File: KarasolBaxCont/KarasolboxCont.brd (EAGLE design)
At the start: 44.1 x 76.2 mm, 28 parts, among them IC1 REG1117, IC2 7808DT, J1 POWER_JACKTOE, Q4 IRF3707S

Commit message: fix
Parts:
- moved CR1 1.27 mm to (30.5, 21.6), turned to 270 degrees
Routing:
- net GND: track 210.1 -> 220.7 mm, vias 1 -> 0
- net D10: track 17.9 -> 13.6 mm
- net VCCSRV: track 82.7 -> 86.8 mm
- net D11: track 19.8 -> 23.5 mm
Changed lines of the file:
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@@
 <element name="PC2" library="SparkFun-Capacitors" package="0805" value="0.1uf" x="26.67" y="59.69" rot="R270"/>
 <element name="CD1" library="SparkFun-DiscreteSemi" package="SMA-DIODE" value="" x="20.32" y="11.43" rot="R180"/>
-<element name="CR1" library="SparkFun-Passives" package="0805" value="1K" x="30.48" y="20.32" rot="R180"/>
+<element name="CR1" library="SparkFun-Passives" package="0805" value="1K" x="30.48" y="21.59" rot="R270"/>
 <element name="PD1" library="SparkFun-DiscreteSemi" package="SMA-DIODE" value="" x="26.67" y="71.12" rot="R90"/>
 <element name="MD2" library="SparkFun-DiscreteSemi" package="SMA-DIODE" value="" x="29.21" y="29.21"/>
@@
 <wire x1="38.8" y1="69.6" x2="39" y2="69.85" width="0.8" layer="1"/>
 <wire x1="38.4" y1="61.2" x2="38.06" y2="60.96" width="0.8" layer="1"/>
-<wire x1="33.6" y1="26.4" x2="35.2" y2="28" width="0.8" layer="1"/>
-<wire x1="33.2" y1="26.4" x2="33.6" y2="26.4" width="0.8" layer="1"/>
-<wire x1="33.2" y1="25.6" x2="33.2" y2="26.4" width="0.8" layer="16"/>
-<wire x1="39.6" y1="19.2" x2="33.4" y2="25.4" width="0.8" layer="16"/>
-<wire x1="33.4" y1="25.4" x2="33.2" y2="25.6" width="0.8" layer="16"/>
-<wire x1="40.4" y1="19.2" x2="39.6" y2="19.2" width="0.8" layer="16"/>
+<wire x1="30.8" y1="23.6" x2="30.8" y2="22.8" width="0.8" layer="1"/>
+<wire x1="35.2" y1="28" x2="30.8" y2="23.6" width="0.8" layer="1"/>
+<wire x1="30.8" y1="22.8" x2="30.48" y2="22.49" width="0.8" layer="1"/>
 <wire x1="35.2" y1="28" x2="35.56" y2="28.31" width="0.8" layer="1"/>
-<wire x1="40.4" y1="19.2" x2="40.64" y2="19.09" width="0.8" layer="16"/>
 <wire x1="31.2" y1="13.2" x2="28" y2="16.4" width="0.8" layer="1"/>
 <wire x1="34.8" y1="13.2" x2="31.2" y2="13.2" width="0.8" layer="1"/>
-<wire x1="40.4" y1="18.8" x2="34.8" y2="13.2" width="0.8" layer="1"/>
+<wire x1="40.4" y1="18.8" x2="38.2" y2="16.6" width="0.8" layer="1"/>
+<wire x1="38.2" y1="16.6" x2="34.8" y2="13.2" width="0.8" layer="1"/>
 <wire x1="28" y1="16.4" x2="27.94" y2="16.51" width="0.8" layer="1"/>
 <wire x1="40.4" y1="18.8" x2="40.64" y2="19.09" width="0.8" layer="1"/>
+<wire x1="32" y1="22.8" x2="30.8" y2="22.8" width="0.8" layer="1"/>
+<wire x1="38.2" y1="16.6" x2="32" y2="22.8" width="0.8" layer="1"/>
 <wire x1="16.8" y1="56.4" x2="16.8" y2="55.2" width="0.8" layer="1"/>
 <wire x1="16.8" y1="55.2" x2="16.8" y2="52.4" width="0.8" layer="1"/>
@@
 <wire x1="8" y1="39.2" x2="7.62" y2="39.37" width="0.8" layer="16"/>
 <wire x1="16" y1="26.8" x2="16.14" y2="26.67" width="0.8" layer="16"/>
-<wire x1="15.6" y1="51.2" x2="31.6" y2="51.2" width="0.8" layer="16"/>
-<wire x1="10" y1="45.6" x2="15.6" y2="51.2" width="0.8" layer="16"/>
-<wire x1="10" y1="40.4" x2="10" y2="45.6" width="0.8" layer="16"/>
+<wire x1="30.4" y1="51.6" x2="31.6" y2="51.6" width="0.8" layer="16"/>
+<wire x1="25.6" y1="56.4" x2="30.4" y2="51.6" width="0.8" layer="16"/>
+<wire x1="24" y1="56.4" x2="25.6" y2="56.4" width="0.8" layer="16"/>
+<wire x1="10" y1="42.4" x2="24" y2="56.4" width="0.8" layer="16"/>
+<wire x1="10" y1="40.4" x2="10" y2="42.4" width="0.8" layer="16"/>
 <wire x1="8.6" y1="39" x2="10" y2="40.4" width="0.8" layer="16"/>
-<wire x1="31.6" y1="51.2" x2="31.735" y2="51.5125" width="0.8" layer="16"/>
+<wire x1="31.6" y1="51.6" x2="31.735" y2="51.5125" width="0.8" layer="16"/>
 <wire x1="10" y1="40.8" x2="10" y2="55.2" width="0.8" layer="1"/>
 <wire x1="8.8" y1="39.6" x2="10" y2="40.8" width="0.8" layer="1"/>
 <wire x1="8" y1="39.6" x2="8.8" y2="39.6" width="0.8" layer="1"/>
 <wire x1="8" y1="39.6" x2="7.62" y2="39.37" width="0.8" layer="1"/>
-<wire x1="32.4" y1="25.2" x2="33.2" y2="25.2" width="0.8" layer="16"/>
-<wire x1="24" y1="16.8" x2="32.4" y2="25.2" width="0.8" layer="16"/>
+<wire x1="26" y1="18.8" x2="40.4" y2="18.8" width="0.8" layer="16"/>
+<wire x1="24" y1="16.8" x2="26" y2="18.8" width="0.8" layer="16"/>
 <wire x1="21.6" y1="16.8" x2="24" y2="16.8" width="0.8" layer="16"/>
 <wire x1="18" y1="20.4" x2="21.6" y2="16.8" width="0.8" layer="16"/>
 <wire x1="18" y1="21.2" x2="18" y2="20.4" width="0.8" layer="16"/>
-<wire x1="33.2" y1="25.2" x2="33.4" y2="25.4" width="0.8" layer="16"/>
+<wire x1="40.4" y1="18.8" x2="40.64" y2="19.09" width="0.8" layer="16"/>
 <wire x1="18" y1="21.2" x2="17.78" y2="21.59" width="0.8" layer="16"/>
 <wire x1="8" y1="60.4" x2="26.4" y2="60.4" width="0.8" layer="1"/>
 <wire x1="26.4" y1="60.4" x2="26.67" y2="60.59" width="0.8" layer="1"/>
-<via x="33.2" y="26.4" extent="1-16" drill="0.8"/>
-<wire x1="32.4" y1="25.2" x2="31.38" y2="20.32" width="0" layer="19" extent="1-16"/>
 </signal>
 <signal name="RAW" class="1">
@@
 <wire x1="13.6" y1="57.2" x2="13.6" y2="57.15" width="0.8" layer="1"/>
 <wire x1="18.8" y1="56.8" x2="19.0754" y2="56.5404" width="0.8" layer="1"/>
-<wire x1="18.8" y1="56.4" x2="18.8" y2="52.4" width="0.8" layer="1"/>
+<wire x1="18.8" y1="56.4" x2="18.8" y2="54" width="0.8" layer="1"/>
+<wire x1="18.8" y1="54" x2="18.8" y2="52.4" width="0.8" layer="1"/>
 <wire x1="18.8" y1="52.4" x2="18.68" y2="52.07" width="0.8" layer="1"/>
 <wire x1="18.8" y1="56.4" x2="19.0754" y2="56.5404" width="0.8" layer="1"/>
@@
 <wire x1="33.8" y1="47.8" x2="35.2" y2="46.4" width="0.8" layer="1"/>
 <wire x1="39.2" y1="48.8" x2="39.355" y2="48.9725" width="0.8" layer="1"/>
-<wire x1="18.8" y1="51.2" x2="18.8" y2="52" width="0.8" layer="1"/>
-<wire x1="16.4" y1="48.8" x2="18.8" y2="51.2" width="0.8" layer="1"/>
-<wire x1="16.4" y1="45.2" x2="16.4" y2="48.8" width="0.8" layer="16"/>
-<wire x1="22" y1="39.6" x2="16.4" y2="45.2" width="0.8" layer="16"/>
-<wire x1="22.8" y1="39.6" x2="22" y2="39.6" width="0.8" layer="16"/>
-<wire x1="18.8" y1="52" x2="18.68" y2="52.07" width="0.8" layer="1"/>
-<wire x1="22.8" y1="39.6" x2="22.86" y2="39.37" width="0.8" layer="16"/>
+<wire x1="24.8" y1="54" x2="18.8" y2="54" width="0.8" layer="1"/>
+<wire x1="24.8" y1="52.4" x2="24.8" y2="54" width="0.8" layer="16"/>
+<wire x1="30.8" y1="46.4" x2="24.8" y2="52.4" width="0.8" layer="16"/>
+<wire x1="32.4" y1="46.4" x2="30.8" y2="46.4" width="0.8" layer="16"/>
+<wire x1="34" y1="48" x2="32.4" y2="46.4" width="0.8" layer="16"/>
+<wire x1="34" y1="48.8" x2="34" y2="48" width="0.8" layer="16"/>
+<wire x1="34" y1="48.8" x2="34.275" y2="48.9725" width="0.8" layer="16"/>
 <wire x1="38.8" y1="24.4" x2="40.4" y2="24.4" width="0.8" layer="16"/>
 <wire x1="24" y1="39.2" x2="38.8" y2="24.4" width="0.8" layer="16"/>
@@
 <wire x1="40.4" y1="24.4" x2="40.64" y2="24.09" width="0.8" layer="16"/>
 <wire x1="23.2" y1="39.2" x2="22.86" y2="39.37" width="0.8" layer="16"/>
-<via x="16.4" y="48.8" extent="1-16" drill="0.8"/>
+<via x="24.8" y="54" extent="1-16" drill="0.8"/>
 </signal>
 <signal name="N$3">
@@
 <contactref element="U$1" pad="D10"/>
 <contactref element="CQ1" pad="1"/>
-<wire x1="24.4" y1="20" x2="29.2" y2="20" width="0.8" layer="1"/>
-<wire x1="23.2" y1="18.8" x2="24.4" y2="20" width="0.8" layer="1"/>
-<wire x1="29.2" y1="20" x2="29.58" y2="20.32" width="0.8" layer="1"/>
-<wire x1="23.2" y1="18.8" x2="22.86" y2="19.05" width="0.8" layer="1"/>
-<wire x1="33.2" y1="21.2" x2="33.2" y2="16.8" width="0.8" layer="1"/>
-<wire x1="32" y1="22.4" x2="33.2" y2="21.2" width="0.8" layer="1"/>
-<wire x1="30.4" y1="22.4" x2="32" y2="22.4" width="0.8" layer="1"/>
-<wire x1="29.6" y1="21.6" x2="30.4" y2="22.4" width="0.8" layer="1"/>
-<wire x1="29.6" y1="20.4" x2="29.6" y2="21.6" width="0.8" layer="1"/>
-<wire x1="33.2" y1="16.8" x2="33.02" y2="16.51" width="0.8" layer="1"/>
-<wire x1="29.6" y1="20.4" x2="29.58" y2="20.32" width="0.8" layer="1"/>
+<wire x1="30.8" y1="18.8" x2="30.8" y2="20.4" width="0.8" layer="1"/>
+<wire x1="32.8" y1="16.8" x2="30.8" y2="18.8" width="0.8" layer="1"/>
+<wire x1="30.8" y1="20.4" x2="30.48" y2="20.69" width="0.8" layer="1"/>
+<wire x1="32.8" y1="16.8" x2="33.02" y2="16.51" width="0.8" layer="1"/>
+<wire x1="25.6" y1="19.2" x2="23.2" y2="19.2" width="0.8" layer="1"/>
+<wire x1="26.8" y1="20.4" x2="25.6" y2="19.2" width="0.8" layer="1"/>
+<wire x1="30.4" y1="20.4" x2="26.8" y2="20.4" width="0.8" layer="1"/>
+<wire x1="23.2" y1="19.2" x2="22.86" y2="19.05" width="0.8" layer="1"/>
+<wire x1="30.4" y1="20.4" x2="30.48" y2="20.69" width="0.8" layer="1"/>
 </signal>
 <signal name="D11">
@@
 <wire x1="35.6" y1="23.2" x2="35.56" y2="23.23" width="0.8" layer="1"/>
 <wire x1="40.4" y1="21.6" x2="40.64" y2="21.59" width="0.8" layer="1"/>
-<wire x1="27.2" y1="21.6" x2="23.2" y2="21.6" width="0.8" layer="1"/>
-<wire x1="29.6" y1="24" x2="27.2" y2="21.6" width="0.8" layer="1"/>
-<wire x1="33.6" y1="24" x2="29.6" y2="24" width="0.8" layer="1"/>
-<wire x1="34.4" y1="23.2" x2="33.6" y2="24" width="0.8" layer="1"/>
-<wire x1="35.2" y1="23.2" x2="34.4" y2="23.2" width="0.8" layer="1"/>
-<wire x1="23.2" y1="21.6" x2="22.86" y2="21.59" width="0.8" layer="1"/>
-<wire x1="35.2" y1="23.2" x2="35.56" y2="23.23" width="0.8" layer="1"/>
+<wire x1="40.4" y1="21.6" x2="23.2" y2="21.6" width="0.8" layer="16"/>
+<wire x1="23.2" y1="21.6" x2="22.86" y2="21.59" width="0.8" layer="16"/>
+<wire x1="40.4" y1="21.6" x2="40.64" y2="21.59" width="0.8" layer="16"/>
 </signal>
 <signal name="D3">
@@
 <wire x1="18.8" y1="47.2" x2="8.4" y2="36.8" width="0.8" layer="1"/>
 <wire x1="18.8" y1="48.8" x2="18.8" y2="47.2" width="0.8" layer="1"/>
-<wire x1="24" y1="54" x2="18.8" y2="48.8" width="0.8" layer="1"/>
-<wire x1="37.6" y1="54" x2="24" y2="54" width="0.8" layer="1"/>
+<wire x1="21.6" y1="51.6" x2="18.8" y2="48.8" width="0.8" layer="1"/>
+<wire x1="28.4" y1="51.6" x2="21.6" y2="51.6" width="0.8" layer="1"/>
+<wire x1="30.8" y1="54" x2="28.4" y2="51.6" width="0.8" layer="1"/>
+<wire x1="37.6" y1="54" x2="30.8" y2="54" width="0.8" layer="1"/>
 <wire x1="39.2" y1="52.4" x2="37.6" y2="54" width="0.8" layer="1"/>
 <wire x1="39.2" y1="51.6" x2="39.2" y2="52.4" width="0.8" layer="1"/>

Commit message: son
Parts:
- added U$2: (no value), Logo:IOTECH_COPPER_M
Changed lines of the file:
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@@
 <element name="CQ1" library="transistor-power" package="D2PACK" value="IRF3707S" x="30.48" y="7.62" rot="R180"/>
 <element name="U$1" library="Arduino-Clk" package="ABK-PRO-MINI" value="ABK-PRO-MINI" x="12.7" y="40.64"/>
+<element name="U$2" library="Logo" package="IOTECH_COPPER_M" value="" x="29.21" y="69.85" rot="MR0"/>
 </elements>
 <signals>

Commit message: value changec
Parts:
- PC2: value 0.1uf -> 100nf
- PC3: value 0.33uf -> 1uf
- PR1: value 330 -> 470
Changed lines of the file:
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@@
 <elements>
 <element name="PC1" library="SparkFun-Capacitors" package="0805" value="10uf" x="17.78" y="52.07"/>
-<element name="PC2" library="SparkFun-Capacitors" package="0805" value="0.1uf" x="26.67" y="59.69" rot="R270"/>
+<element name="PC2" library="SparkFun-Capacitors" package="0805" value="100nf" x="26.67" y="59.69" rot="R270"/>
 <element name="CD1" library="SparkFun-DiscreteSemi" package="SMA-DIODE" value="" x="20.32" y="11.43" rot="R180"/>
 <element name="CR1" library="SparkFun-Passives" package="0805" value="1K" x="30.48" y="21.59" rot="R270"/>
@@
 <element name="MR2" library="SparkFun-Passives" package="0805" value="4700" x="35.56" y="29.21" rot="R90"/>
 <element name="TR1" library="SparkFun-Passives" package="0805" value="4700" x="35.56" y="24.13" rot="R90"/>
-<element name="PR1" library="SparkFun-Passives" package="0805" value="330" x="12.7" y="57.15"/>
+<element name="PR1" library="SparkFun-Passives" package="0805" value="470" x="12.7" y="57.15"/>
 <element name="WIFI" library="esp8266modules" package="ESP01" value="ESP01" x="35.56" y="57.15"/>
 <element name="S1" library="switch-misc" package="9077-2" value="9077-2" x="19.05" y="71.12"/>
@@
 <element name="Q4" library="transistor-power" package="D2PACK" value="IRF3707S" x="15.24" y="12.7" rot="MR180"/>
 <element name="IC2" library="linear" package="TO252" value="7808DT" x="35.56" y="60.96" rot="R270"/>
-<element name="PC3" library="SparkFun-Capacitors" package="0805" value="0.33uf" x="38.1" y="69.85" rot="R180"/>
+<element name="PC3" library="SparkFun-Capacitors" package="0805" value="1uf" x="38.1" y="69.85" rot="R180"/>
 <element name="CQ1" library="transistor-power" package="D2PACK" value="IRF3707S" x="30.48" y="7.62" rot="R180"/>
 <element name="U$1" library="Arduino-Clk" package="ABK-PRO-MINI" value="ABK-PRO-MINI" x="12.7" y="40.64"/>

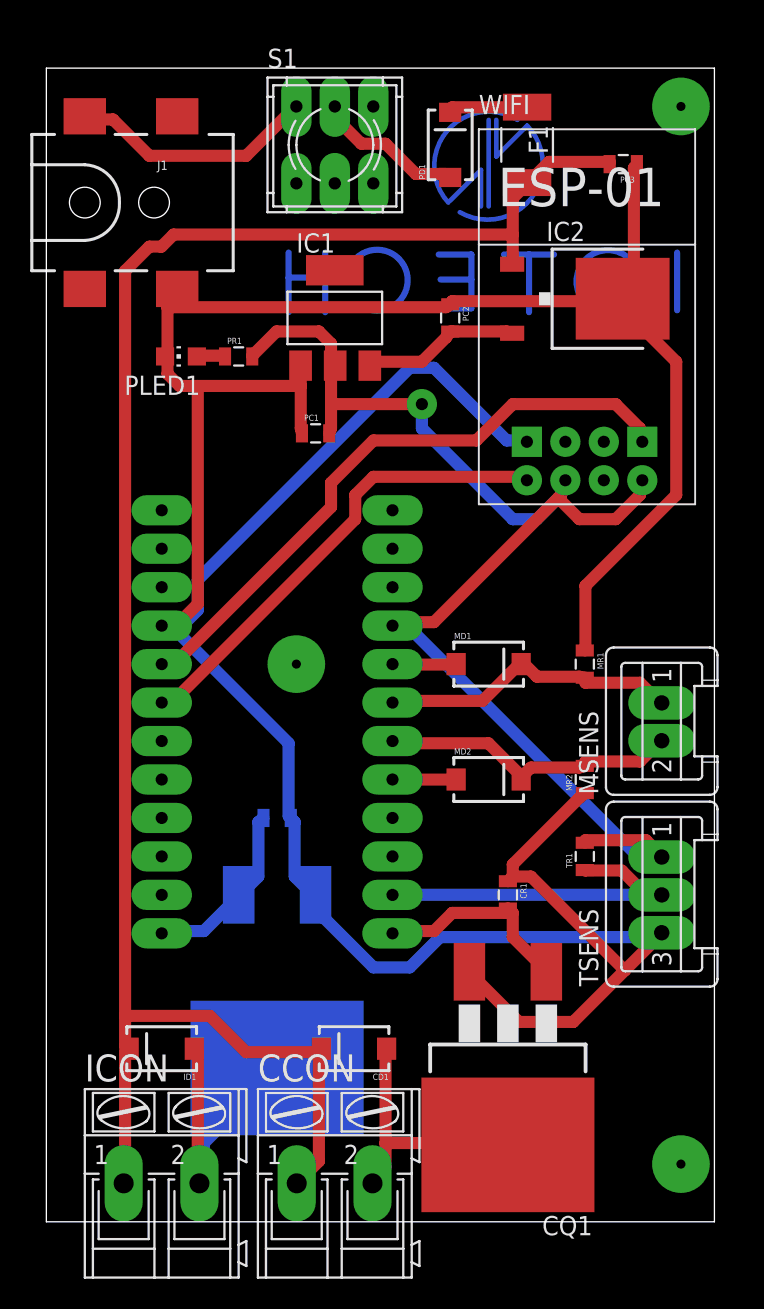
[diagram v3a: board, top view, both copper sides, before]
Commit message: ptototip 2 için son ayarlar
bağlantı yerleri ve mosfet çıkış diyod yeri düzenlendi. izole
kalınlştırıldı.
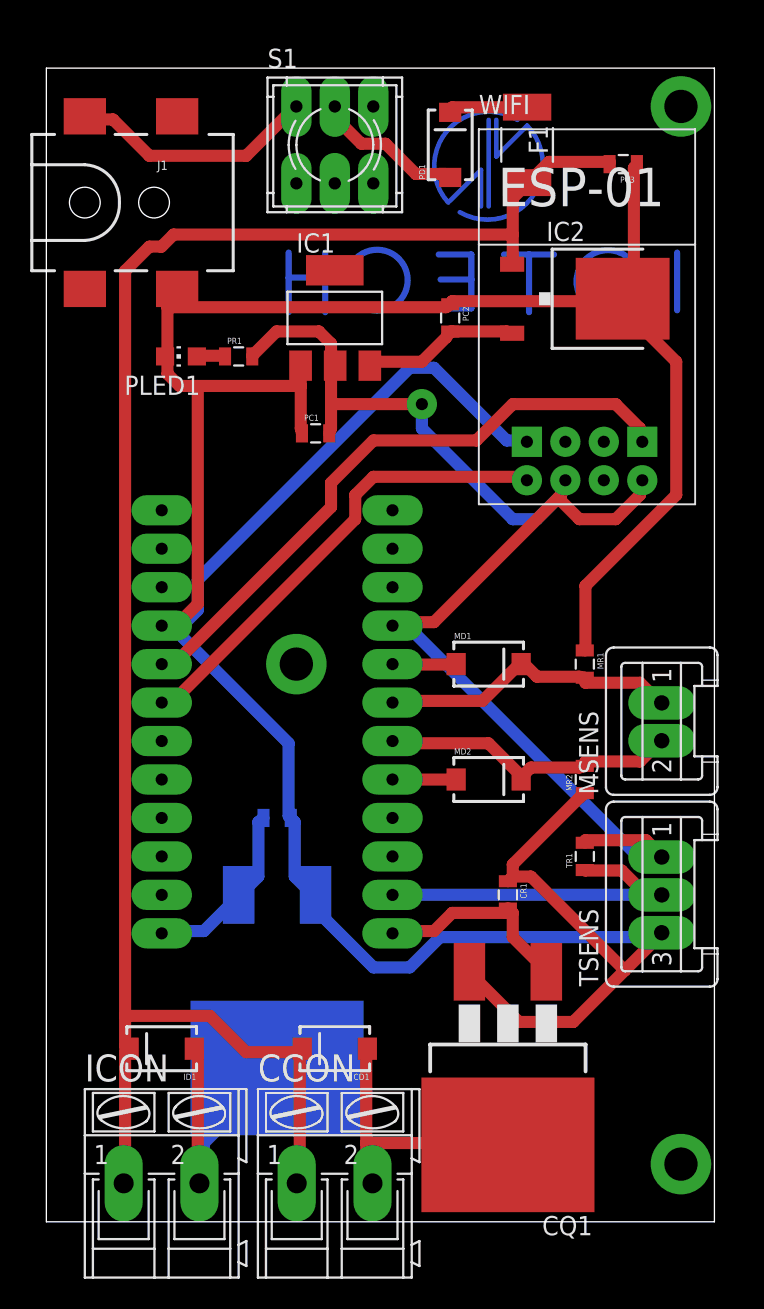
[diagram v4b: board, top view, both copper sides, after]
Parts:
- moved CD1 1.27 mm to (19.1, 11.4)
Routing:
- net RAW: track 122.6 -> 121.3 mm
- net N$2: track 17.4 -> 18.4 mm
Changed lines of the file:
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@@
 <?xml version="1.0" encoding="utf-8"?>
 <!DOCTYPE eagle SYSTEM "eagle.dtd">
-<eagle version="8.1.0">
+<eagle version="8.1.1">
 <drawing>
 <settings>
@@
 <element name="PC1" library="SparkFun-Capacitors" package="0805" value="10uf" x="17.78" y="52.07"/>
 <element name="PC2" library="SparkFun-Capacitors" package="0805" value="100nf" x="26.67" y="59.69" rot="R270"/>
-<element name="CD1" library="SparkFun-DiscreteSemi" package="SMA-DIODE" value="" x="20.32" y="11.43" rot="R180"/>
+<element name="CD1" library="SparkFun-DiscreteSemi" package="SMA-DIODE" value="" x="19.05" y="11.43" rot="R180"/>
 <element name="CR1" library="SparkFun-Passives" package="0805" value="1K" x="30.48" y="21.59" rot="R270"/>
 <element name="PD1" library="SparkFun-DiscreteSemi" package="SMA-DIODE" value="" x="26.67" y="71.12" rot="R90"/>
@@
 <contactref element="IC2" pad="1"/>
 <contactref element="PC3" pad="2"/>
-<wire x1="18" y1="4" x2="18" y2="11.2" width="0.8" layer="1"/>
-<wire x1="16.8" y1="2.8" x2="18" y2="4" width="0.8" layer="1"/>
-<wire x1="18" y1="11.2" x2="18.17" y2="11.43" width="0.8" layer="1"/>
+<wire x1="16.73" y1="4" x2="16.73" y2="11.2" width="0.8" layer="1"/>
+<wire x1="16.8" y1="2.8" x2="16.73" y2="4" width="0.8" layer="1"/>
+<wire x1="16.73" y1="11.2" x2="16.9" y2="11.43" width="0.8" layer="1"/>
 <wire x1="16.8" y1="2.8" x2="16.5354" y2="2.54" width="0.8" layer="1"/>
 <wire x1="33.2" y1="70" x2="37.2" y2="70" width="0.8" layer="1"/>
@@
 <wire x1="5.2" y1="13.6" x2="5.2" y2="62.8" width="0.8" layer="1"/>
 <wire x1="5.2" y1="11.6" x2="5.47" y2="11.43" width="0.8" layer="1"/>
-<wire x1="13.2" y1="11.2" x2="17.6" y2="11.2" width="0.8" layer="1"/>
+<wire x1="13.2" y1="11.2" x2="16.33" y2="11.2" width="0.8" layer="1"/>
+<wire x1="16.73" y1="11.2" x2="16.33" y2="11.2" width="0.8" layer="1"/>
 <wire x1="10.8" y1="13.6" x2="13.2" y2="11.2" width="0.8" layer="1"/>
 <wire x1="5.2" y1="13.6" x2="10.8" y2="13.6" width="0.8" layer="1"/>
-<wire x1="17.6" y1="11.2" x2="18.17" y2="11.43" width="0.8" layer="1"/>
+<wire x1="16.33" y1="11.2" x2="16.9" y2="11.43" width="0.8" layer="1"/>
 </signal>
 <signal name="D9">
@@
 <contactref element="CQ1" pad="2"/>
 <contactref element="CD1" pad="A"/>
-<wire x1="22.4" y1="3.6" x2="22.4" y2="5.2" width="0.8" layer="1"/>
-<wire x1="22.4" y1="5.2" x2="22.4" y2="11.2" width="0.8" layer="1"/>
-<wire x1="21.6" y1="2.8" x2="22.4" y2="3.6" width="0.8" layer="1"/>
-<wire x1="22.4" y1="11.2" x2="22.47" y2="11.43" width="0.8" layer="1"/>
+<wire x1="21.13" y1="3.6" x2="21.13" y2="5.2" width="0.8" layer="1"/>
+<wire x1="21.13" y1="5.2" x2="21.13" y2="11.2" width="0.8" layer="1"/>
+<wire x1="21.6" y1="2.8" x2="21.13" y2="3.6" width="0.8" layer="1"/>
+<wire x1="21.13" y1="11.2" x2="21.2" y2="11.43" width="0.8" layer="1"/>
 <wire x1="21.6" y1="2.8" x2="21.5392" y2="2.54" width="0.8" layer="1"/>
-<wire x1="30.4" y1="5.2" x2="22.4" y2="5.2" width="0.8" layer="1"/>
+<wire x1="30.4" y1="5.2" x2="21.13" y2="5.2" width="0.8" layer="1"/>
 <wire x1="30.4" y1="5.2" x2="30.48" y2="5.08" width="0.8" layer="1"/>
 </signal>
@@
 </signal>
 <signal name="N$4">
-<via x="16.51" y="36.83" extent="1-16" drill="0.6" diameter="3.81" shape="octagon"/>
+<via x="16.51" y="36.83" extent="1-16" drill="2.2" diameter="4"/>
 </signal>
 <signal name="N$8">
-<via x="41.91" y="3.81" extent="1-16" drill="0.6" diameter="3.81" shape="octagon"/>
+<via x="41.91" y="3.81" extent="1-16" drill="2.2" diameter="4"/>
 </signal>
 <signal name="N$9">
-<via x="41.91" y="73.66" extent="1-16" drill="0.6" diameter="3.81" shape="octagon"/>
+<via x="41.91" y="73.66" extent="1-16" drill="2.2" diameter="4"/>
 </signal>
 <signal name="N$1">
